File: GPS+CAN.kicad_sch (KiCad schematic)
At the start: 1 part, among them U1 MCP25625x-x-ML

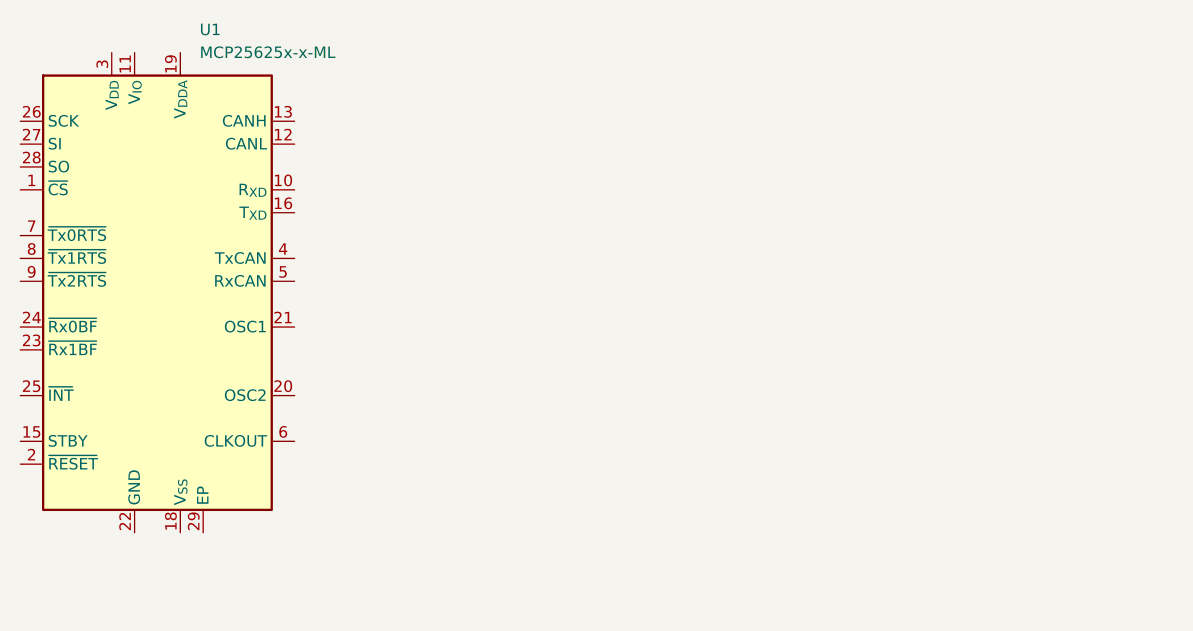
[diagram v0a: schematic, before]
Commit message: Added footprints
Added the schematics + footprints for current forerunners of GPS antenna and receiver
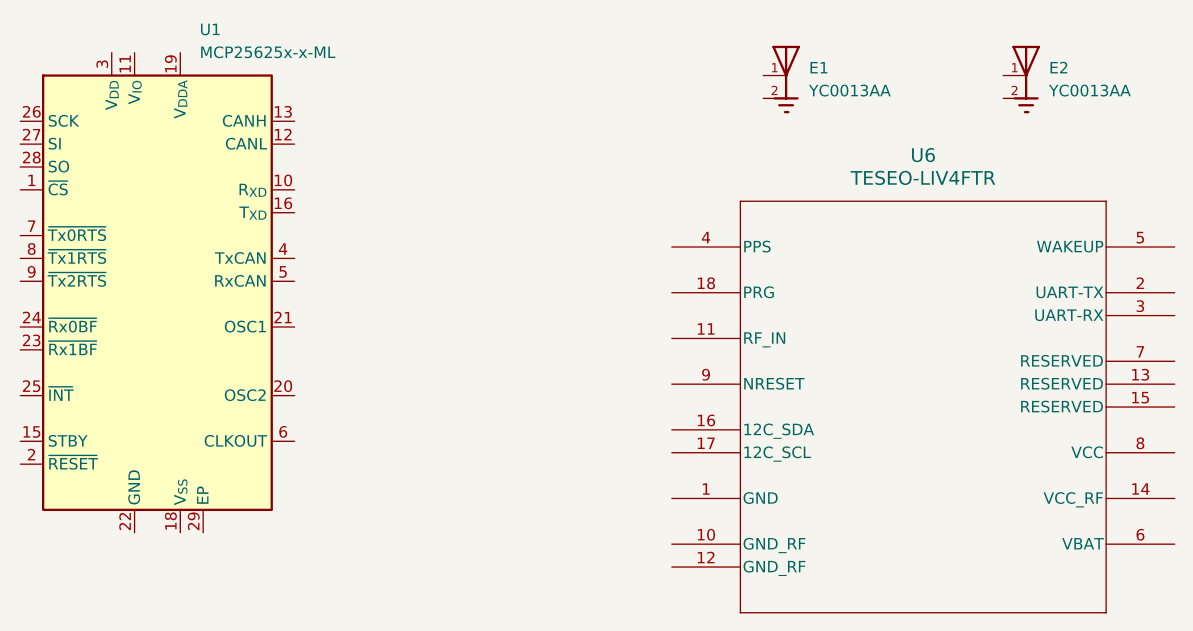
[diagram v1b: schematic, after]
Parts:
- added E1, E2: YC0013AA, YC0013AA:XCVR_YC0013AA, symbol YC0013AA:YC0013AA
- added U6: TESEO-LIV4FTR, LCC-18_STM, symbol 2026-06-19_06-08-10:TESEO-LIV4FTR
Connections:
- new net: E1.2, E1.3
- new net: E2.2, E2.3
